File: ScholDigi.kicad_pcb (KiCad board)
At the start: 2 copper layers, 66 x 49 mm, 61 parts, among them J1 USB_C_Receptacle_PowerOnly_6P, J2 USB_C_Receptacle_USB2.0_14P, J3 Battery JST, J4 GPS Antenna coaxial, Q1 FS8205A, SW1 Boot Button, SW2 Reset Button, U1 ESP32-C6-MINI-1, U2 MAX-M10S, U3 TP4056-42-ESOP8, U4 DW01A, U5 TPS63060, U6 CP2102

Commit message: Add little kitty
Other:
- board text added: "/\___/\ / \ l u u l l * l \ w / - Meow! ===== / \ __ l l\ \ l l/ / -Olin- l l l l / \ ml lm /_/"
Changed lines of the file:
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@@
 		(layer "Edge.Cuts")
+	)
+	(gr_text "    /\\___/\\\n   /       \\\n  l  u   u  l\n  l    *    l\n   \\   w   /     - Meow!\n    =====\n   /       \\ __\n   l        l\\ \\\n   l        l/ /   -Olin-\n   l  l l   l /\n   \\ ml lm /_/"
+		(at 146.5 61.5 0)
+		(layer "F.SilkS")
+		(effects
+			(font
+				(size 0.5 0.5)
+				(thickness 0.0625)
+				(bold yes)
+			)
+			(justify left bottom)
+		)
 	)
 	(segment

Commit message: Button Text
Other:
- board text added: "Boot"
- board text added: "RST"
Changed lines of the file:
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@@
 		(tags "resistor")
 		(property "Reference" "R2"
-			(at -1 -1.5 0)
+			(at -2.5 -1 0)
 			(layer "F.SilkS")
 			(effects
@@
 			)
 			(justify left bottom)
+		)
+	)
+	(gr_text "Boot"
+		(at 112.5 81 0)
+		(layer "F.SilkS")
+		(effects
+			(font
+				(size 1 1)
+				(thickness 0.1)
+			)
+			(justify left bottom)
+		)
+	)
+	(gr_text "RST"
+		(at 126 81 0)
+		(layer "F.SilkS")
+		(effects
+			(font
+				(size 1 1)
+				(thickness 0.1)
+			)
+			(justify left bottom)

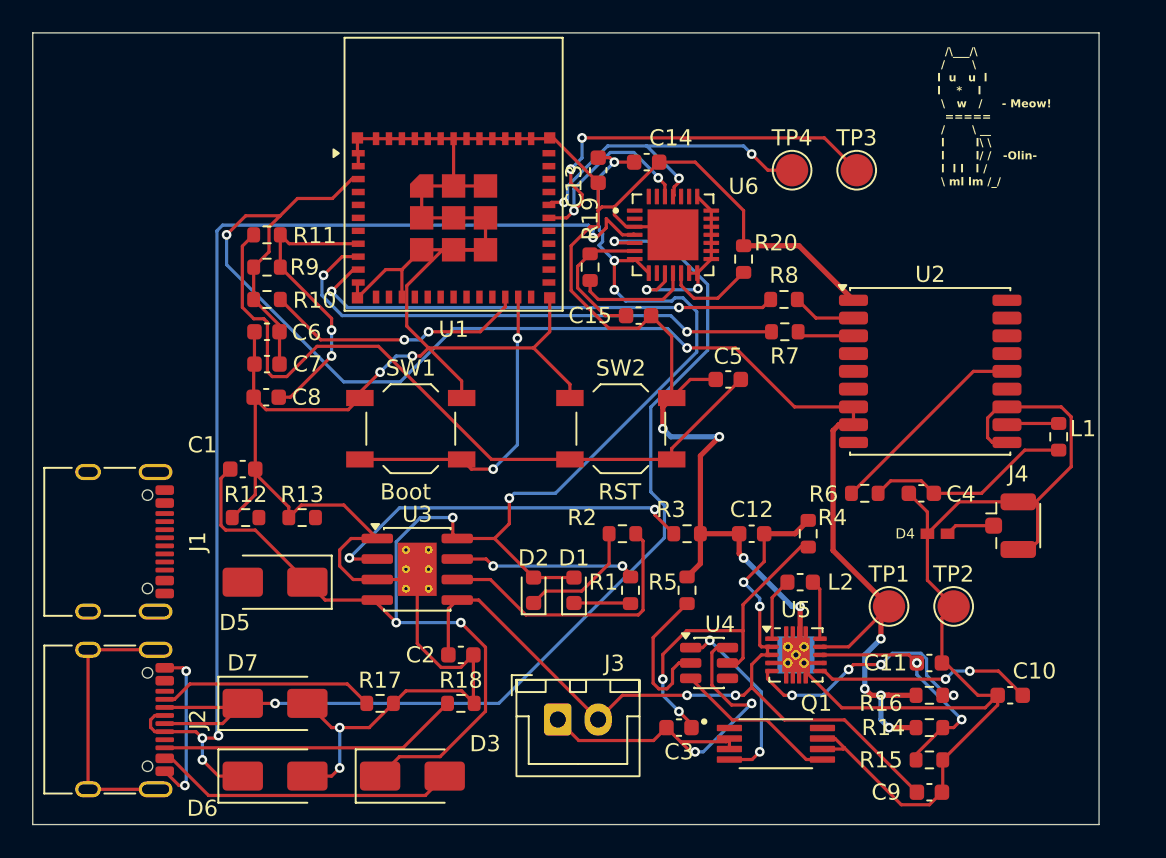
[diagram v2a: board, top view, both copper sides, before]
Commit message: Mounting holes
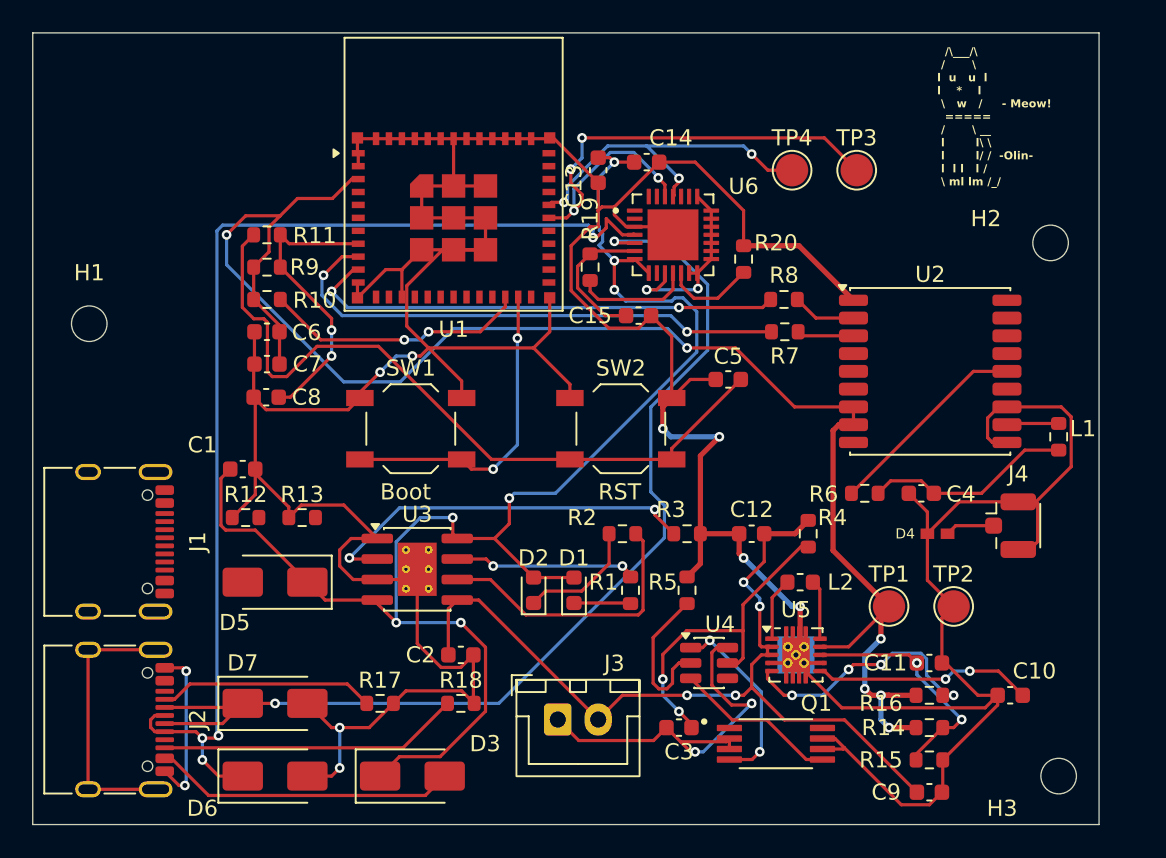
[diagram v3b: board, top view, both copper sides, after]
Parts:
- added H1: MountingHole_2.2mm_M2, MountingHole:MountingHole_2.2mm_M2, F.Cu at (94.5, 70.0)
- added H2: MountingHole_2.2mm_M2, MountingHole:MountingHole_2.2mm_M2, F.Cu at (154.0, 65.0)
- added H3: MountingHole_2.2mm_M2, MountingHole:MountingHole_2.2mm_M2, F.Cu at (154.5, 98.0)

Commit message: No drc errors now
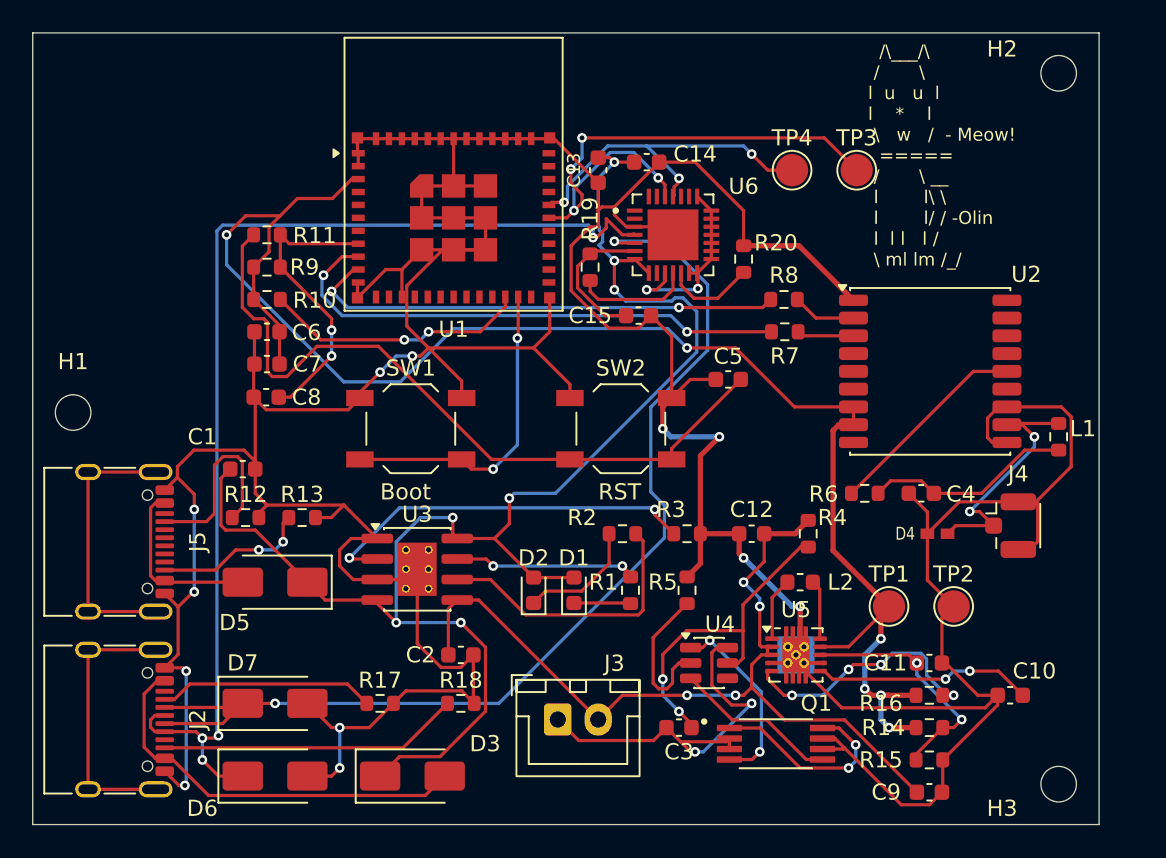
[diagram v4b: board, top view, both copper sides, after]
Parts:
- removed J1: USB_C_Receptacle_PowerOnly_6P, Connector_USB:USB_C_Receptacle_XKB_U262-16XN-4BVC11
- added J5: USB_C_Receptacle_USB2.0_14P, Connector_USB:USB_C_Receptacle_XKB_U262-16XN-4BVC11, F.Cu at (95.5, 83.5)
- moved H2 10.5 mm to (154.5, 54.5)
- moved H1 5.59 mm to (93.5, 75.5)
- moved H3 0.50 mm to (154.5, 98.5)
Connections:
- R12 pad 1: VIN- -> Net-(J5-CC1)
- R12 pad 2: Net-(J1-CC2) -> VIN-
- R13 pad 1: VIN- -> Net-(J5-CC2)
- R13 pad 2: Net-(J1-CC1) -> VIN-
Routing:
- net VIN-: track 311.2 -> 331.7 mm, vias 10 -> 12
- net unconnected-(J5-SHIELD-PadSH): track 0.00 -> 17.0 mm
- net Net-(Q1-Pad1): track 0.00 -> 12.5 mm, vias 0 -> 2
- net Net-(J5-CC1): track 0.00 -> 12.1 mm
- net Net-(D5-A): track 0.00 -> 11.1 mm
- net Net-(J4-In): track 6.29 -> 16.4 mm, vias 0 -> 2
- net Net-(J5-CC2): track 0.00 -> 9.70 mm, vias 0 -> 2
- net Net-(D3-A): track 18.8 -> 25.2 mm
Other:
- board text added: "/\___/\ / \ l u u l l * l \ w / - Meow! ===== / \ __ l l\ \ l l/ / -Olin l l l l / \ ml lm /_/"
- board text removed: "/\___/\ / \ l u u l l * l \ w / - Meow! ===== / \ __ l l\ \ l l/ / -Olin- l l l l / \ ml lm /_/"

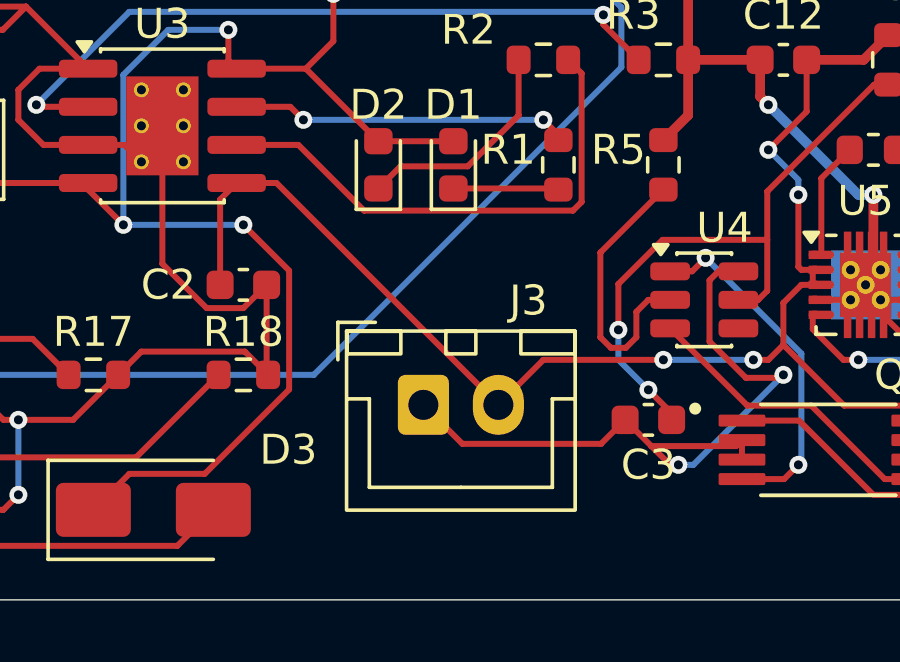
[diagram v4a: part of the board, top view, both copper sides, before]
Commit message: change jst connector
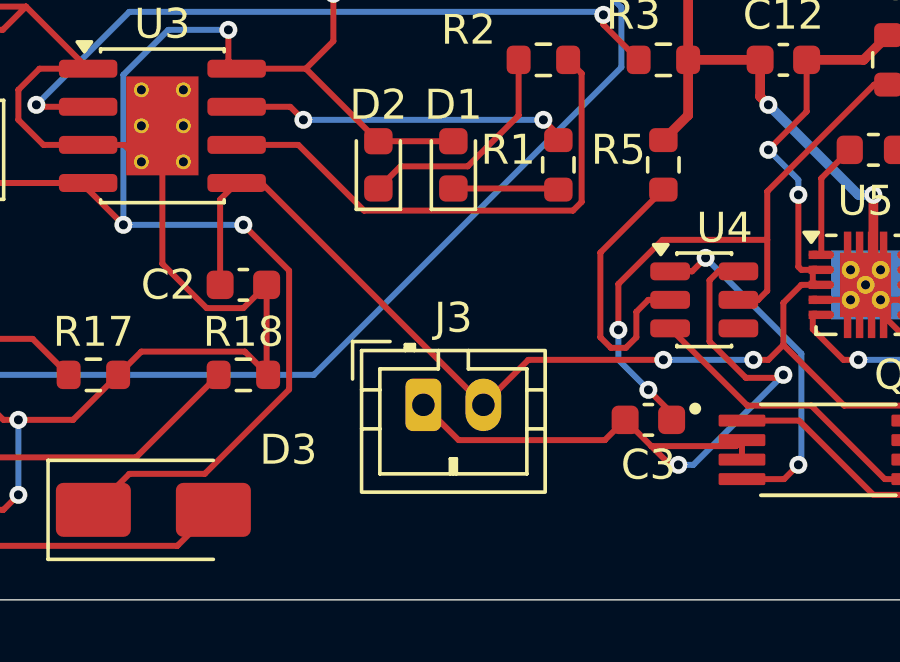
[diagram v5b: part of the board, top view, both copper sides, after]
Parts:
- J3: footprint Connector_JST:JST_XH_B2B-XH-A_1x02_P2.50mm_Vertical -> Connector_JST:JST_PH_B2B-PH-K_1x02_P2.00mm_Vertical
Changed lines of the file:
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@@
 		)
 	)
-	(footprint "Connector_JST:JST_XH_B2B-XH-A_1x02_P2.50mm_Vertical"
+	(footprint "Connector_JST:JST_PH_B2B-PH-K_1x02_P2.00mm_Vertical"
 		(layer "F.Cu")
 		(at 123.5 94.5)
-		(descr "JST XH series connector, B2B-XH-A (http://www.jst-mfg.com/product/pdf/eng/eXH.pdf)")
-		(tags "connector JST XH vertical")
+		(descr "JST PH series connector, B2B-PH-K (http://www.jst-mfg.com/product/pdf/eng/ePH.pdf)")
+		(tags "connector JST PH vertical")
 		(property "Reference" "J3"
-			(at 3.5 -3.475 0)
+			(at 1 -2.9 0)
 			(layer "F.SilkS")
 			(effects
@@
 		)
 		(property "Value" "Battery JST"
-			(at 1.25 4.6 0)
+			(at 1 4 0)
 			(layer "F.Fab")
 			(effects
@@
 		(duplicate_pad_numbers_are_jumpers no)
 		(fp_line
-			(start -2.85 -2.75)
-			(end -2.85 -1.5)
+			(start -2.36 -2.11)
+			(end -2.36 -0.86)
 			(stroke
 				(width 0.12)
@@
 		)
 		(fp_line
-			(start -2.55 -0.2)
-			(end -1.8 -0.2)
+			(start -2.06 -0.5)
+			(end -1.45 -0.5)
 			(stroke
 				(width 0.12)
@@
 		)
 		(fp_line
-			(start -1.8 -0.2)
-			(end -1.8 2.75)
+			(start -2.06 0.8)
+			(end -1.45 0.8)
 			(stroke
 				(width 0.12)
@@
 		)
 		(fp_line
-			(start -1.8 2.75)
-			(end 1.25 2.75)
+			(start -1.45 -1.2)
+			(end -1.45 2.3)
 			(stroke
 				(width 0.12)
@@
 		)
 		(fp_line
-			(start -1.6 -2.75)
-			(end -2.85 -2.75)
+			(start -1.45 2.3)
+			(end 3.45 2.3)
 			(stroke
 				(width 0.12)
@@
 		)
 		(fp_line
-			(start 4.3 -0.2)
-			(end 4.3 2.75)
+			(start -1.11 -2.11)
+			(end -2.36 -2.11)
 			(stroke
 				(width 0.12)
@@
 		)
 		(fp_line
-			(start 4.3 2.75)
-			(end 1.25 2.75)
+			(start -0.6 -2.01)
+			(end -0.6 -1.81)
 			(stroke
 				(width 0.12)
@@
 		)
 		(fp_line
-			(start 5.05 -0.2)
-			(end 4.3 -0.2)
+			(start -0.3 -2.01)
+			(end -0.6 -2.01)
 			(stroke
 				(width 0.12)
@@
 			(layer "F.SilkS")
 		)
-		(fp_rect
-			(start -2.56 -2.46)
-			(end 5.06 3.51)
+		(fp_line
+			(start -0.3 -1.91)
+			(end -0.6 -1.91)
 			(stroke
 				(width 0.12)
 				(type solid)
 			)
-			(fill no)
 			(layer "F.SilkS")
 		)
-		(fp_rect
-			(start -2.55 -2.45)
-			(end -0.75 -1.7)
+		(fp_line
+			(start -0.3 -1.81)
+			(end -0.3 -2.01)
 			(stroke
 				(width 0.12)
 				(type solid)
 			)
-			(fill no)
 			(layer "F.SilkS")
 		)
-		(fp_rect
-			(start 0.75 -2.45)
-			(end 1.75 -1.7)
+		(fp_line
+			(start 0.5 -1.81)
+			(end 0.5 -1.2)
+			(stroke
+				(width 0.12)
+				(type solid)
+			)
+			(layer "F.SilkS")
+		)
+		(fp_line
+			(start 0.5 -1.2)
+			(end -1.45 -1.2)
+			(stroke
+				(width 0.12)
+				(type solid)
+			)
+			(layer "F.SilkS")
+		)
+		(fp_line
+			(start 0.9 1.8)
+			(end 1.1 1.8)
+			(stroke
+				(width 0.12)
+				(type solid)
+			)
+			(layer "F.SilkS")
+		)
+		(fp_line
+			(start 0.9 2.3)
+			(end 0.9 1.8)
+			(stroke
+				(width 0.12)
+				(type solid)
+			)
+			(layer "F.SilkS")
+		)
+		(fp_line
+			(start 1 2.3)
+			(end 1 1.8)
+			(stroke
+				(width 0.12)
+				(type solid)
+			)
+			(layer "F.SilkS")
+		)
+		(fp_line
+			(start 1.1 1.8)
+			(end 1.1 2.3)
+			(stroke
+				(width 0.12)
+				(type solid)
+			)
+			(layer "F.SilkS")
+		)
+		(fp_line
+			(start 1.5 -1.2)
+			(end 1.5 -1.81)
+			(stroke
+				(width 0.12)
+				(type solid)
+			)
+			(layer "F.SilkS")
+		)
+		(fp_line
+			(start 3.45 -1.2)
+			(end 1.5 -1.2)
+			(stroke
+				(width 0.12)
+				(type solid)
+			)
+			(layer "F.SilkS")
+		)
+		(fp_line
+			(start 3.45 2.3)
+			(end 3.45 -1.2)
+			(stroke
+				(width 0.12)
+				(type solid)
+			)
+			(layer "F.SilkS")
+		)
+		(fp_line
+			(start 4.06 -0.5)
+			(end 3.45 -0.5)
+			(stroke
+				(width 0.12)
+				(type solid)
+			)
+			(layer "F.SilkS")
+		)
+		(fp_line
+			(start 4.06 0.8)
+			(end 3.45 0.8)
 			(stroke
 				(width 0.12)
 				(type solid)
 			)
-			(fill no)
 			(layer "F.SilkS")
 		)
 		(fp_rect
-			(start 3.25 -2.45)
-			(end 5.05 -1.7)
+			(start -2.06 -1.81)
+			(end 4.06 2.91)
 			(stroke
 				(width 0.12)
@@
 		)
 		(fp_rect
-			(start -2.95 -2.85)
-			(end 5.45 3.9)
+			(start -2.45 -2.2)
+			(end 4.45 3.3)
 			(stroke
 				(width 0.05)
@@
 		)
 		(fp_line
-			(start -0.625 -2.35)
-			(end 0 -1.35)
+			(start -2.36 -2.11)
+			(end -2.36 -0.86)
 			(stroke
 				(width 0.1)
@@
 		)
 		(fp_line
-			(start 0 -1.35)
-			(end 0.625 -2.35)
+			(start -1.11 -2.11)
+			(end -2.36 -2.11)
 			(stroke
 				(width 0.1)
@@
 		)
 		(fp_rect
-			(start -2.45 -2.35)
-			(end 4.95 3.4)
+			(start -1.95 -1.7)
+			(end 3.95 2.8)
 			(stroke
 				(width 0.1)
@@
 		)
 		(fp_text user "${REFERENCE}"
-			(at 1.25 2.7 0)
+			(at 1 1.5 0)
 			(layer "F.Fab")
 			(effects
@@
 		(pad "1" thru_hole roundrect
 			(at 0 0)
-			(size 1.7 2)
-			(drill 1)
+			(size 1.2 1.75)
+			(drill 0.75)
 			(layers "*.Cu" "*.Mask")
 			(remove_unused_layers no)
-			(roundrect_rratio 0.147059)
+			(roundrect_rratio 0.208333)
 			(net "BAT-")
 			(pinfunction "Pin_1_1")
@@
 		)
 		(pad "2" thru_hole oval
-			(at 2.5 0)
-			(size 1.7 2)
-			(drill 1)
+			(at 2 0)
+			(size 1.2 1.75)
+			(drill 0.75)
 			(layers "*.Cu" "*.Mask")
 			(remove_unused_layers no)
@@
 		)
 		(embedded_fonts no)
-		(model "${KICAD10_3DMODEL_DIR}/Connector_JST.3dshapes/JST_XH_B2B-XH-A_1x02_P2.50mm_Vertical.step"
+		(model "${KICAD10_3DMODEL_DIR}/Connector_JST.3dshapes/JST_PH_B2B-PH-K_1x02_P2.00mm_Vertical.step"
 			(offset
 				(xyz 0 0 0)
@@
 	)
 	(segment
-		(start 129.425 95.8)
-		(end 124.8 95.8)
+		(start 130.225 95)
+		(end 129.55 95.675)
+		(width 0.2)
+		(layer "F.Cu")
+		(net "BAT-")
+	)
+	(segment
+		(start 129.55 95.675)
+		(end 124.675 95.675)
 		(width 0.2)
 		(layer "F.Cu")
@@
 	)
 	(segment
-		(start 130.225 95)
-		(end 129.425 95.8)
-		(width 0.2)
-		(layer "F.Cu")
-		(net "BAT-")
-	)
-	(segment
-		(start 124.8 95.8)
+		(start 124.675 95.675)
 		(end 123.5 94.5)
 		(width 0.2)
@@
 	)
 	(segment
+		(start 127 93)
+		(end 131.5 93)
+		(width 0.2)
+		(layer "F.Cu")
+		(net "BAT+")
+	)
+	(segment
 		(start 134.5 93)
 		(end 135 93)
@@
 	)
 	(segment
-		(start 127.5 93)
-		(end 131.5 93)
-		(width 0.2)
-		(layer "F.Cu")
-		(net "BAT+")
-	)
-	(segment
 		(start 145.725 99)
 		(end 141.25 94.525)
@@
 	)
 	(segment
-		(start 126 94.5)
-		(end 118.605 87.105)
+		(start 136.275 84.725)
+		(end 136.275 83)
 		(width 0.2)
 		(layer "F.Cu")
@@
 	)
 	(segment
-		(start 136.275 84.725)
-		(end 136.275 83)
+		(start 118.105 87.105)
+		(end 125.5 94.5)
 		(width 0.2)
 		(layer "F.Cu")
@@
 	)
 	(segment
-		(start 126 94.5)
-		(end 127.5 93)
+		(start 117.275 87.105)
+		(end 118.105 87.105)
 		(width 0.2)
 		(layer "F.Cu")
@@
 	)
 	(segment
-		(start 137.525 94.525)
-		(end 135.5 92.5)
+		(start 125.5 94.5)
+		(end 127 93)
 		(width 0.2)
 		(layer "F.Cu")
@@
 	)
 	(segment
-		(start 118.605 87.105)
-		(end 117.275 87.105)
+		(start 137.525 94.525)
+		(end 135.5 92.5)
 		(width 0.2)
 		(layer "F.Cu")

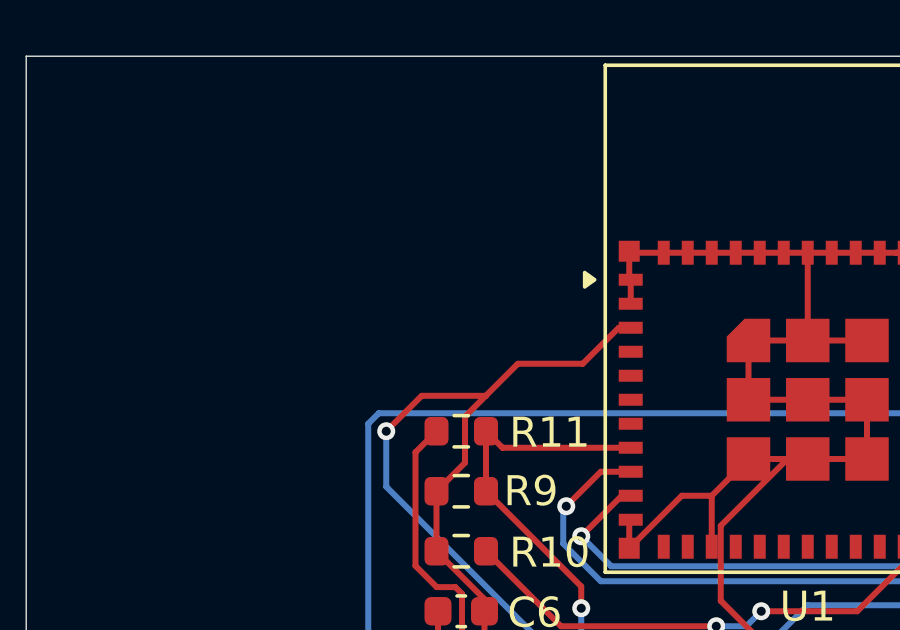
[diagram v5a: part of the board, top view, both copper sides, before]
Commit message: Rah, testpoints for display
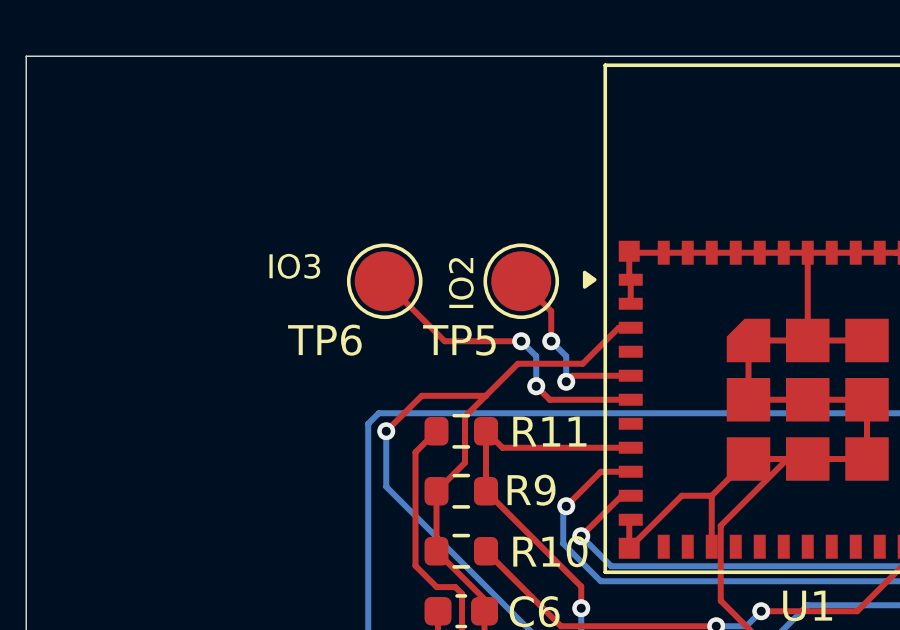
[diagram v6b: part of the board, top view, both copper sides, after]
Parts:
- added TP5: IO2, TestPoint:TestPoint_Pad_D2.0mm, F.Cu at (107.5, 59.5)
- added TP6: IO3, TestPoint:TestPoint_Pad_D2.0mm, F.Cu at (103.0, 59.5)
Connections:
- U1 pad 5: unconnected-(U1-IO2-Pad5) -> IO2
- U1 pad 6: unconnected-(U1-IO3-Pad6) -> IO3
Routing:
- net IO3: track 0.00 -> 10.4 mm, vias 0 -> 2
- net IO2: track 0.00 -> 6.20 mm, vias 0 -> 2
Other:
- board text added: "IO2"
- board text added: "IO3"

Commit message: Change
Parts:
- removed TP5: IO2, TestPoint:TestPoint_Pad_D2.0mm
- removed TP6: IO3, TestPoint:TestPoint_Pad_D2.0mm
- added J1: Conn_01x04, Connector_PinHeader_2.54mm:PinHeader_1x04_P2.54mm_Vertical, F.Cu at (97.4, 60.0)
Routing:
- net VIN-: track 331.7 -> 345.2 mm
- net +3V3: track 100.7 -> 106.5 mm
- net IO2: track 6.20 -> 7.91 mm
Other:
- board text added: "3v3"
- board text added: "GND"
